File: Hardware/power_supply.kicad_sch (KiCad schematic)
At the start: 27 parts, among them J1 Conn_01x02_Pin, U1 MIC26903YJL-TR, U2 LD39200PU33R, U3 INA226

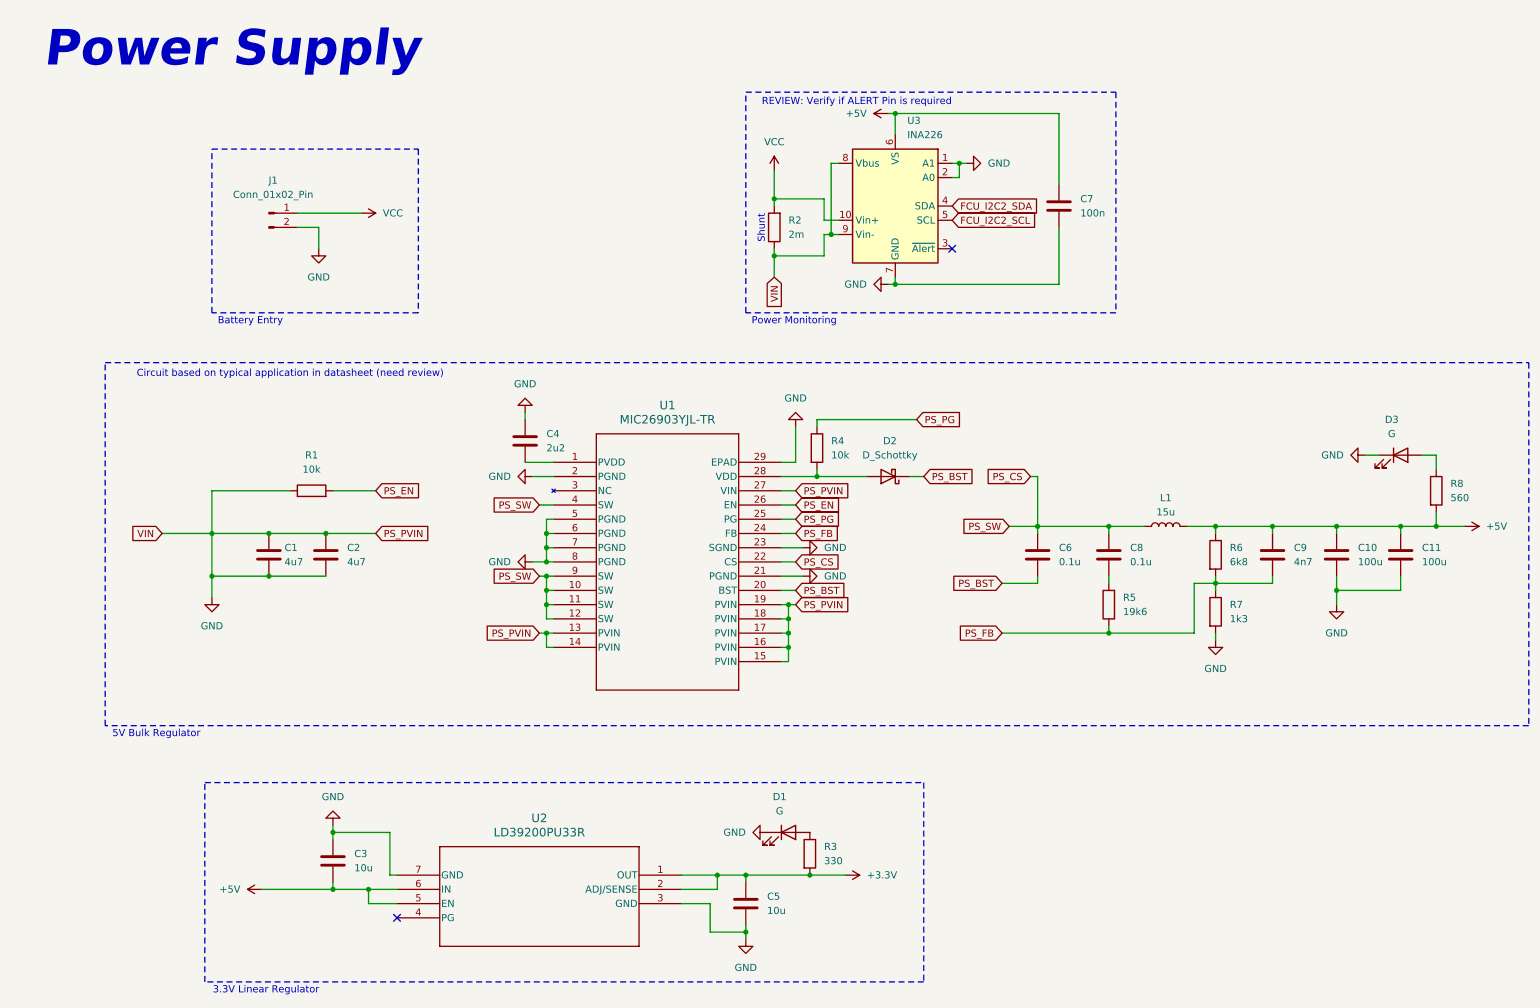
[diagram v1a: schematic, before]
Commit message: board placement, no trails, just pain
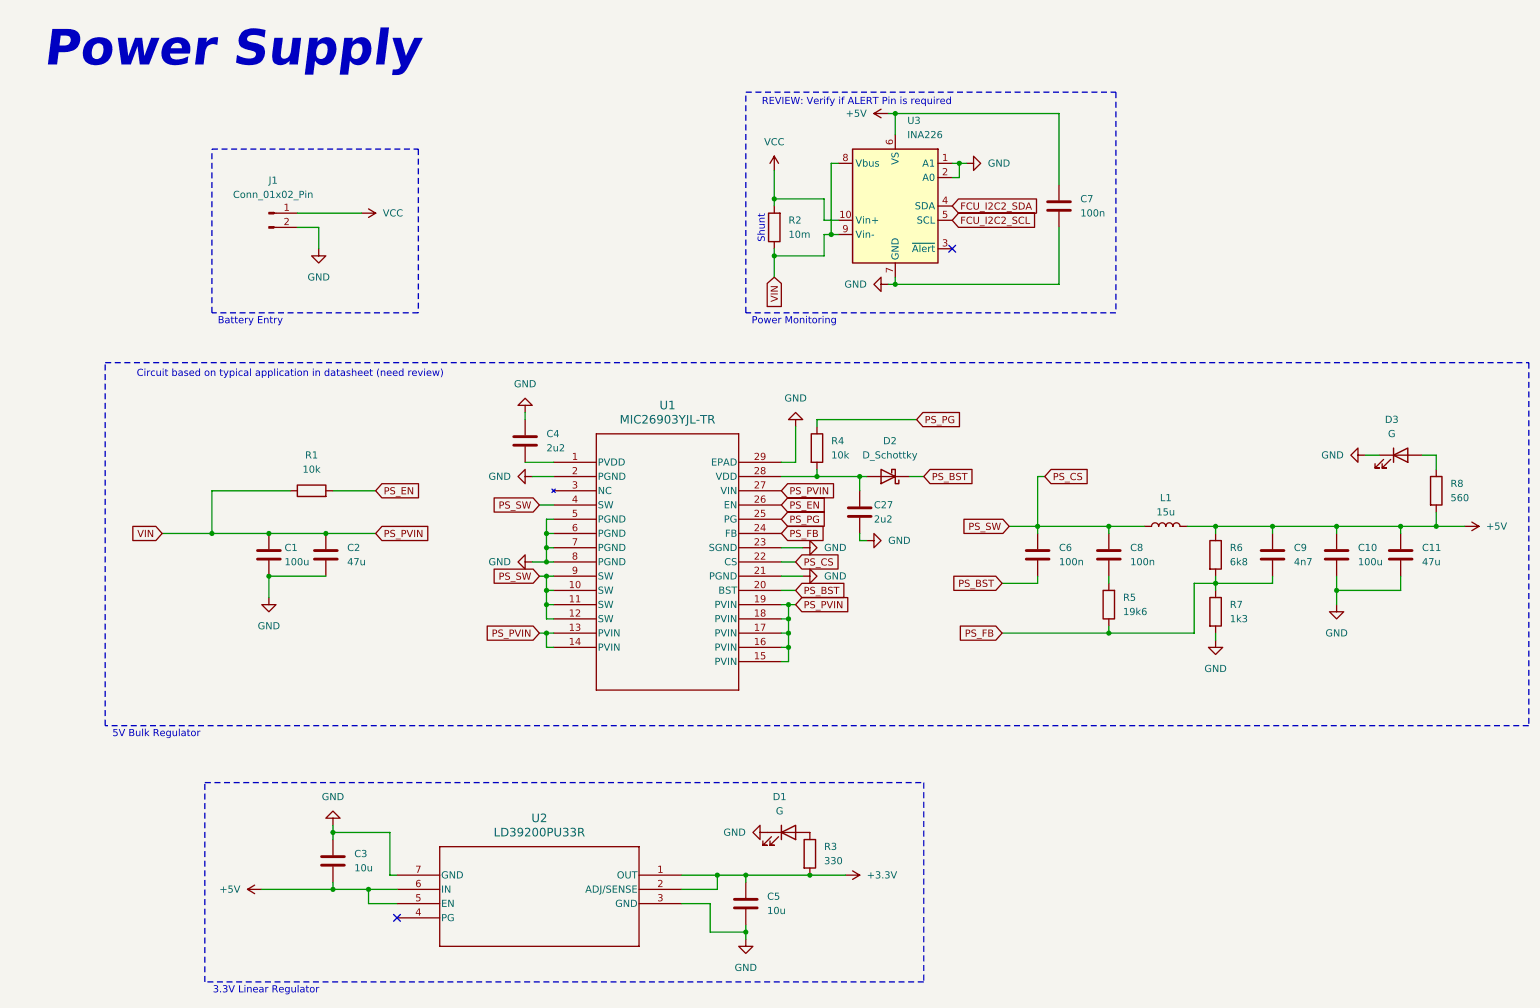
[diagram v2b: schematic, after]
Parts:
- added C27: 2u2, Capacitor_SMD:C_0805_2012Metric_Pad1.18x1.45mm_HandSolder, symbol Device:C
- C1: value 4u7 -> 100u; footprint (none) -> Capacitor_SMD:C_Elec_6.3x7.7; Digikey_Link (none) -> https://www.digikey.com.br/pt/products/detail/kemet/A768EB1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; MPN (none) -> A768EB107M1ELAS036
- C10: footprint (none) -> Capacitor_SMD:C_Elec_6.3x7.7; Digikey_Link (none) -> https://www.digikey.com.br/pt/products/detail/kemet/A768EB1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; MPN (none) -> A768EB107M1ELAS036
- C11: value 100u -> 47u; footprint (none) -> Capacitor_SMD:C_1206_3216Metric_Pad1.33x1.80mm_HandSolder; Digikey_Link (none) -> https://www.digikey.com.br/pt/products/detail/tdk-corporati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; MPN (none) -> C3216X5R1E476M160AC
- C2: value 4u7 -> 47u; footprint (none) -> Capacitor_SMD:C_1206_3216Metric_Pad1.33x1.80mm_HandSolder; Digikey_Link (none) -> https://www.digikey.com.br/pt/products/detail/tdk-corporati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; MPN (none) -> C3216X5R1E476M160AC
- C3, C5: footprint (none) -> Capacitor_SMD:C_0805_2012Metric_Pad1.18x1.45mm_HandSolder; Digikey_Link (none) -> https://www.digikey.com.br/pt/products/detail/samsung-elect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; MPN (none) -> CL21B106KPQNNNE
- C4: footprint (none) -> Capacitor_SMD:C_0805_2012Metric_Pad1.18x1.45mm_HandSolder; Digikey_Link (none) -> https://www.digikey.com.br/pt/products/detail/kyocera-avx/0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; MPN (none) -> 08053C225KAT2A
- C6, C8: value 0.1u -> 100n; footprint (none) -> Capacitor_SMD:C_0603_1608Metric_Pad1.08x0.95mm_HandSolder; Digikey_Link (none) -> https://www.digikey.com.br/pt/products/detail/kemet/C0603C1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; MPN (none) -> C0603C104K3RACTU
- C7: footprint Capacitor_SMD:C_0603_1608Metric -> Capacitor_SMD:C_0603_1608Metric_Pad1.08x0.95mm_HandSolder; Digikey_Link (none) -> https://www.digikey.com.br/pt/products/detail/kemet/C0603C1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; MPN (none) -> C0603C104K3RACTU
- C9: footprint (none) -> Capacitor_SMD:C_0603_1608Metric_Pad1.08x0.95mm_HandSolder; Digikey_Link (none) -> https://www.digikey.com.br/pt/products/detail/kemet/C0603C4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; MPN (none) -> C0603C472F3GACTU
- D1, D3: footprint LED_SMD:LED_0603_1608Metric -> LED_SMD:LED_0603_1608Metric_Pad1.05x0.95mm_HandSolder; Digikey_Link (none) -> https://www.digikey.com.br/pt/products/detail/liteon/LTST-S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; MPN (none) -> LTST-S270KGKT
- D2: Digikey_Link (none) -> https://www.digikey.com.br/pt/products/detail/evvo/sd103aws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; MPN (none) -> SD103AWS
- J1: footprint (none) -> Connector_AMASS:AMASS_XT60-M_1x02_P7.20mm_Vertical; Digikey_Link (none) -> https://www.digikey.com/en/products/detail/sparkfun-electro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; MPN (none) -> 11864
- L1: footprint (none) -> Aircraft_Footprints:IND_PA4343_FOOTPRINT2_PUL; Digikey_Link (none) -> https://www.digikey.com.br/pt/products/detail/pulse-electro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; MPN (none) -> PA4343-103ANLT
- R1, R4: footprint (none) -> Resistor_SMD:R_0603_1608Metric_Pad0.98x0.95mm_HandSolder; Digikey_Link (none) -> https://www.digikey.com.br/pt/products/detail/yageo/RC0603F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; MPN (none) -> RC0603FR-0710KL
- R2: value 2m -> 10m; footprint (none) -> Resistor_SMD:R_2512_6332Metric_Pad1.40x3.35mm_HandSolder; Digikey_Link (none) -> https://www.digikey.com.br/pt/products/detail/bourns-inc/CR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; MPN (none) -> CRF2512-FZ-R010ELF
- R3: Digikey_Link (none) -> https://www.digikey.com.br/pt/products/detail/yageo/RC0603J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; MPN (none) -> RC0603JR-07330RL
- R5: footprint (none) -> Resistor_SMD:R_0603_1608Metric_Pad0.98x0.95mm_HandSolder; Digikey_Link (none) -> https://www.digikey.com.br/pt/products/detail/vishay-dale/C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; MPN (none) -> CRCW060319K6FKEAC
- R6: footprint (none) -> Resistor_SMD:R_0603_1608Metric_Pad0.98x0.95mm_HandSolder; Digikey_Link (none) -> https://www.digikey.com.br/pt/products/detail/yageo/RC0603J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; MPN (none) -> RC0603JR-076K8L
- R7: footprint (none) -> Resistor_SMD:R_0603_1608Metric_Pad0.98x0.95mm_HandSolder; Digikey_Link (none) -> https://www.digikey.com.br/pt/products/detail/yageo/RC0603J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; MPN (none) -> RC0603JR-071K3L
- R8: Digikey_Link (none) -> https://www.digikey.com.br/pt/products/detail/stackpole-ele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; MPN (none) -> RMCF0603FT560R
- U1: Digikey_Link (none) -> https://www.digikey.com.br/pt/products/detail/microchip-tec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; MPN (none) -> MIC26903YJL-TR
- U2: Digikey_Link (none) -> https://www.digikey.com.br/pt/products/detail/stmicroelectr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; MPN (none) -> LD39200PU33R
- U3: Digikey_Link (none) -> https://www.digikey.com.br/pt/products/detail/texas-instrum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; MPN (none) -> INA226AIDGST
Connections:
- net GND: now also C27.2; no longer C1.1, C2.1, R1.1, R2.1, U1.13 (PVIN), U1.14 (PVIN), U1.15 (PVIN), U1.16 (PVIN), U1.17 (PVIN), U1.18 (PVIN), U1.19 (PVIN), U1.27 (VIN), U3.8 (Vbus), U3.9 (Vin-)
- net at D2.2 (A), R4.2, U1.28 (VDD): now also C27.1
- new net PS_PVIN: C1.1, C2.1, R1.1, R2.1, U1.13 (PVIN), U1.14 (PVIN), U1.15 (PVIN), U1.16 (PVIN), U1.17 (PVIN), U1.18 (PVIN), U1.19 (PVIN), U1.27 (VIN), U3.8 (Vbus), U3.9 (Vin-)
